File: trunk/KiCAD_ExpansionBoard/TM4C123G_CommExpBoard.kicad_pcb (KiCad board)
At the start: 2 copper layers, 50.8 x 58.4 mm, 58 parts, among them J1 TI_BOOSTER_40_J1, J2 TI_BOOSTER_40_J2, J3 TI_BOOSTER_40_J3, J4 TI_BOOSTER_40_J4, P1 ANT_GND, P10 GPIO0, P5 ANT_C, P6 CAN, P7 UART1, P8 RS485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

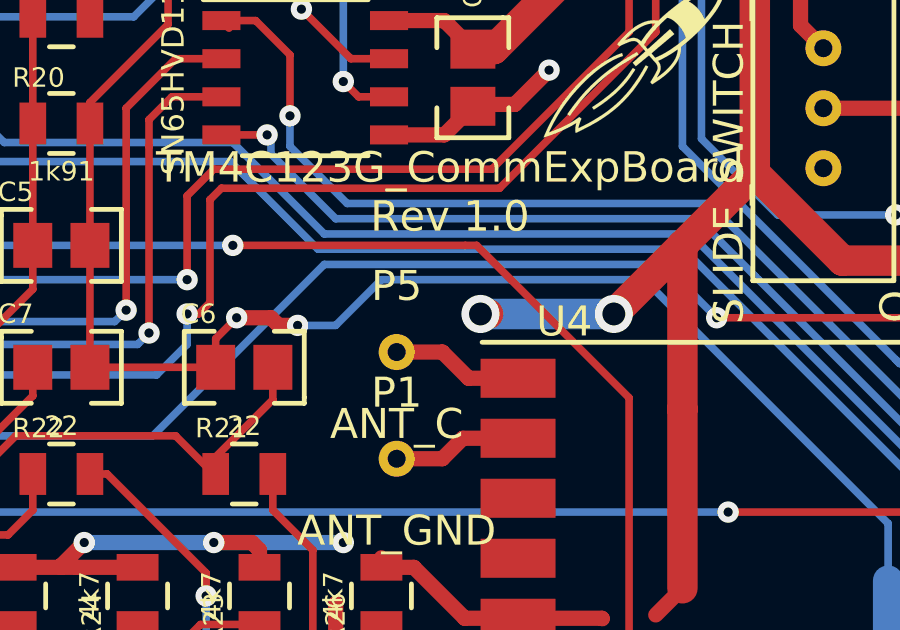
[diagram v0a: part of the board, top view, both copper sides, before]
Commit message: moved P1 and P5 silkscreens near relative pads.
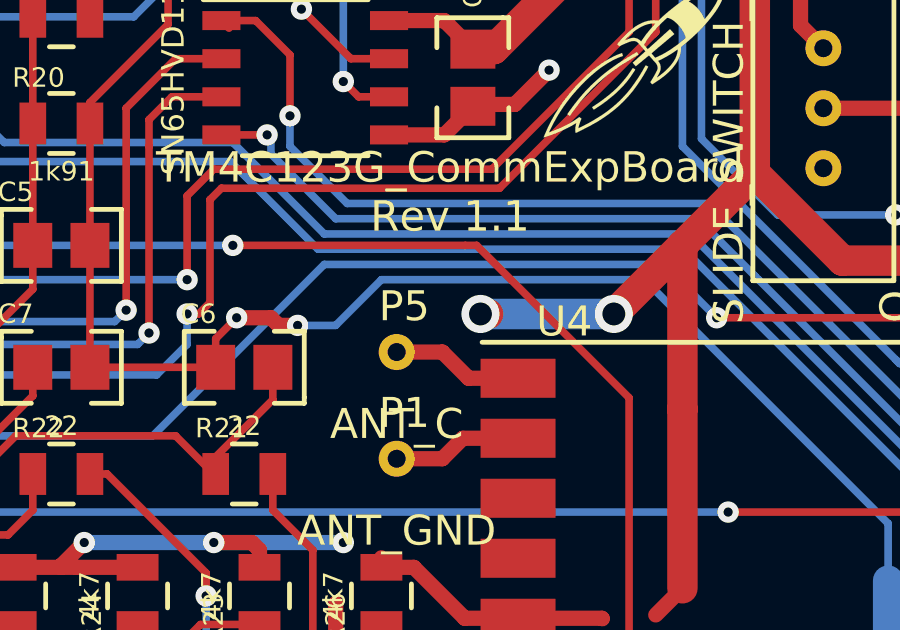
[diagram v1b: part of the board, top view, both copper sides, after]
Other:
- board text added: "TM4C123G_CommExpBoard Rev 1.1"
- board text removed: "TM4C123G_CommExpBoard Rev 1.0"
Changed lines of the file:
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@@
     (links 139)
     (no_connects 0)
-    (area 125.649999 57.069999 176.610001 115.650001)
+    (area 108.280288 51.989999 181.690001 123.604001)
     (thickness 1.6)
     (drawings 57)
@@
   (title_block
     (title "TM4C123G Communication Expansion Board")
-    (rev 1.0)
+    (rev 1.1)
     (company "Luca Buccolini, Student @ Università Politecnica delle Marche")
     (comment 1 "Expansion Board for the Texas Instruments TM4C123G Launchpad ")
@@
   (module ANT_PAD_MD (layer F.Cu)
     (at 147.066 102.362)
-    (fp_text reference P1 (at 0 -2.2) (layer F.SilkS)
+    (fp_text reference P1 (at 0.254 -1.524) (layer F.SilkS)
       (effects (font (size 1 1) (thickness 0.15)))
     )
@@
   (module ANT_PAD_MD (layer F.Cu)
     (at 147.066 98.806)
-    (fp_text reference P5 (at 0 -2.2) (layer F.SilkS)
+    (fp_text reference P5 (at 0.254 -1.524) (layer F.SilkS)
       (effects (font (size 1 1) (thickness 0.15)))
     )
@@
     (effects (font (size 0.762 0.762) (thickness 0.15875)))
   )
-  (gr_text "TM4C123G_CommExpBoard \nRev 1.0" (at 148.844 93.472) (layer F.SilkS)
+  (gr_text "TM4C123G_CommExpBoard \nRev 1.1" (at 148.844 93.472) (layer F.SilkS)
     (effects (font (size 1.016 1.016) (thickness 0.15875)))
   )

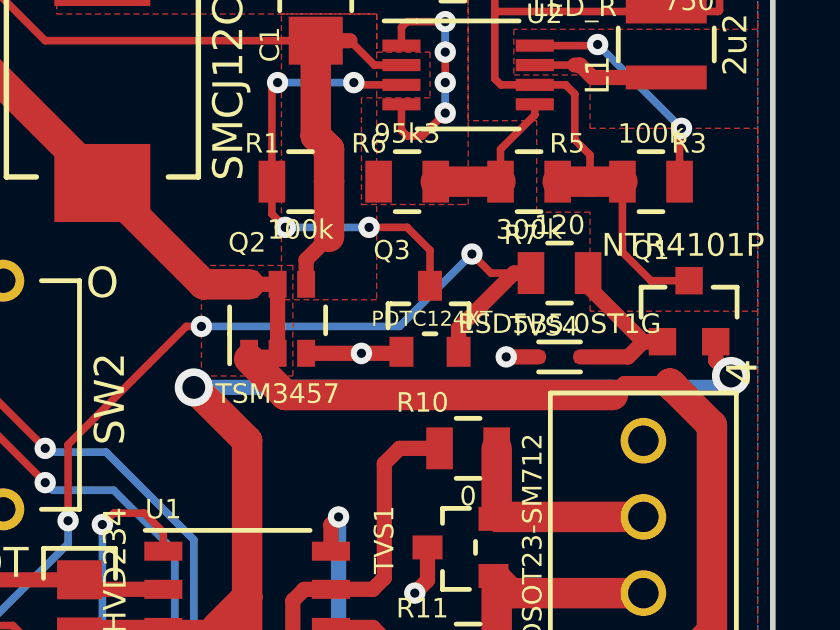
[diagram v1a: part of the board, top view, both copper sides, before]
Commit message: Update of PCB and schematic to rev 1.1 (fixed old Q3 footprint in which pins 1 and 2 were flipped and relative nets). Build new v1.1 fabrication files.
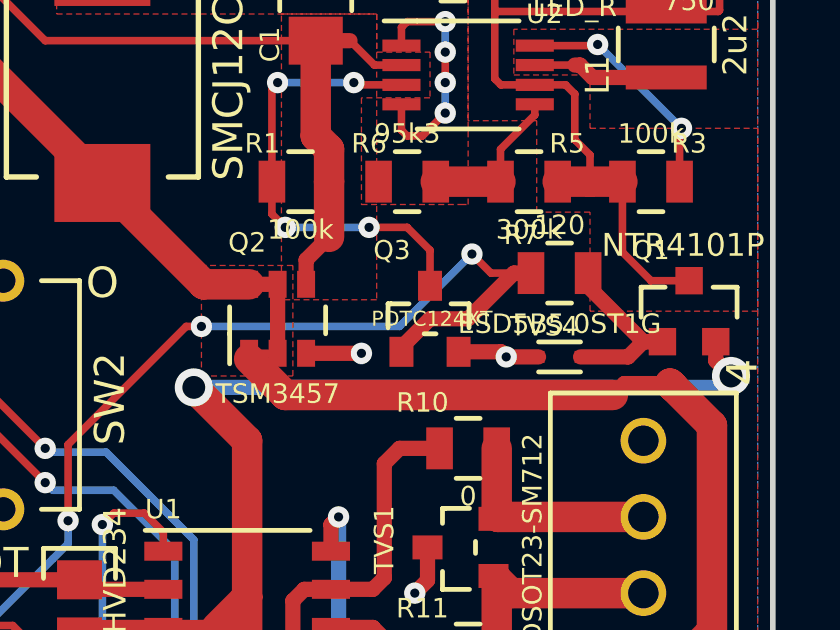
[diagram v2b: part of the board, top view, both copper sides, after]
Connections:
- Q3 pad 1: GND -> +5V_TLP
- Q3 pad 2: +5V_TLP -> GND
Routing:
- net +5V_TLP: track 52.8 -> 54.3 mm
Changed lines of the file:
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@@
     (thickness 1.6)
     (drawings 57)
-    (tracks 732)
+    (tracks 734)
     (zones 0)
     (modules 58)
@@
   (layers
     (15 F.Cu signal)
-    (0 B.Cu signal)
+    (0 B.Cu signal hide)
     (16 B.Adhes user)
     (17 F.Adhes user)
@@
       (drillshape 0)
       (scaleselection 1)
-      (outputdirectory PCB_fabrication/Drill/))
+      (outputdirectory PCB_fabrication/Gerber/))
   )
   (net 0 "")
@@
     (pad 2 smd rect (at 0.9525 1.09982) (size 0.8001 1.00076)
       (layers F.Cu F.Paste F.Mask)
-      (net 3 +5V_TLP)
+      (net 43 GND)
     )
     (pad 1 smd rect (at -0.9525 1.09982) (size 0.8001 1.00076)
       (layers F.Cu F.Paste F.Mask)
-      (net 43 GND)
+      (net 3 +5V_TLP)
     )
     (model smd\SOT23_3.wrl
@@
   (segment (start 156.21 81.661) (end 153.7335 81.661) (width 0.508) (layer F.Cu) (net 2))
   (segment (start 153.7335 81.661) (end 153.416 81.9785) (width 0.508) (layer F.Cu) (net 2))
-  (segment (start 148.59 84.582) (end 149.352 84.582) (width 0.254) (layer F.Cu) (net 3))
   (segment (start 152.527 79.375) (end 153.035 78.867) (width 0.254) (layer B.Cu) (net 3))
   (segment (start 153.035 78.867) (end 153.035 78.105) (width 0.254) (layer B.Cu) (net 3))
@@
   (segment (start 150.368 81.534) (end 152.527 79.375) (width 0.254) (layer B.Cu) (net 3))
   (segment (start 150.368 82.55) (end 150.368 81.534) (width 0.254) (layer B.Cu) (net 3))
+  (segment (start 164.1475 72.47382) (end 164.1475 72.3265) (width 0.508) (layer F.Cu) (net 3))
+  (segment (start 167.894 69.85) (end 168.4655 69.85) (width 0.508) (layer F.Cu) (net 3))
+  (segment (start 166.37 71.374) (end 167.894 69.85) (width 0.508) (layer F.Cu) (net 3))
+  (segment (start 165.1 71.374) (end 166.37 71.374) (width 0.508) (layer F.Cu) (net 3))
+  (segment (start 164.1475 72.3265) (end 165.1 71.374) (width 0.508) (layer F.Cu) (net 3))
+  (segment (start 148.59 84.582) (end 149.352 84.582) (width 0.254) (layer F.Cu) (net 3))
   (segment (start 150.368 82.55) (end 150.368 82.55) (width 0.254) (layer B.Cu) (net 3))
   (via (at 150.368 82.55) (size 0.7112) (layers F.Cu B.Cu) (net 3))
@@
   (segment (start 141.351 84.582) (end 138.303 87.63) (width 0.254) (layer B.Cu) (net 3))
   (segment (start 130.81 87.63) (end 138.303 87.63) (width 0.254) (layer B.Cu) (net 3))
-  (segment (start 166.0525 72.47382) (end 166.0525 71.6915) (width 0.508) (layer F.Cu) (net 3))
-  (segment (start 166.0525 71.6915) (end 167.894 69.85) (width 0.508) (layer F.Cu) (net 3))
-  (segment (start 167.894 69.85) (end 168.4655 69.85) (width 0.508) (layer F.Cu) (net 3))
   (segment (start 161.798 82.931) (end 163.195 82.931) (width 0.254) (layer F.Cu) (net 4))
   (segment (start 172.72 99.06) (end 173.99 100.33) (width 0.254) (layer F.Cu) (net 4))
@@
   (segment (start 131.318 102.87) (end 133.604 100.584) (width 0.254) (layer F.Cu) (net 42))
   (segment (start 130.81 102.87) (end 130.81 102.87) (width 0.254) (layer F.Cu) (net 42))
+  (segment (start 166.0525 72.47382) (end 167.46982 72.47382) (width 0.508) (layer F.Cu) (net 43))
+  (via (at 167.64 72.644) (size 0.7112) (layers F.Cu B.Cu) (net 43))
+  (segment (start 167.64 72.644) (end 168.718 72.644) (width 0.508) (layer F.Cu) (net 43))
+  (segment (start 167.46982 72.47382) (end 167.64 72.644) (width 0.508) (layer F.Cu) (net 43))
+  (via (at 162.814 72.524) (size 0.7112) (layers F.Cu B.Cu) (net 43))
+  (segment (start 162.814 72.524) (end 162.814 72.644) (width 0.508) (layer B.Cu) (net 43))
   (segment (start 163.449 106.426) (end 163.449 104.521) (width 0.254) (layer B.Cu) (net 43))
   (segment (start 142.875 97.663) (end 143.129 97.917) (width 0.508) (layer F.Cu) (net 43))
@@
   (segment (start 156.21 80.391) (end 153.7335 80.391) (width 0.508) (layer F.Cu) (net 43))
   (segment (start 153.7335 80.391) (end 153.416 80.0735) (width 0.508) (layer F.Cu) (net 43))
-  (segment (start 168.718 72.644) (end 167.64 72.644) (width 0.508) (layer F.Cu) (net 43))
-  (via (at 167.64 72.644) (size 0.7112) (layers F.Cu B.Cu) (net 43))
-  (via (at 162.814 72.524) (size 0.7112) (layers F.Cu B.Cu) (net 43))
-  (segment (start 162.814 72.524) (end 162.814 72.644) (width 0.508) (layer B.Cu) (net 43))
   (segment (start 165.01618 78.994) (end 165.01618 80.09382) (width 0.508) (layer F.Cu) (net 43))
   (via (at 164.592 80.518) (size 0.7112) (layers F.Cu B.Cu) (net 43))
   (segment (start 165.01618 80.09382) (end 164.592 80.518) (width 0.508) (layer F.Cu) (net 43))
   (segment (start 160.97 72.524) (end 162.814 72.524) (width 0.508) (layer F.Cu) (net 43))
-  (segment (start 162.814 72.524) (end 164.09732 72.524) (width 0.508) (layer F.Cu) (net 43))
-  (segment (start 164.09732 72.524) (end 164.1475 72.47382) (width 0.508) (layer F.Cu) (net 43))
   (segment (start 164.1475 62.2681) (end 164.1475 61.6585) (width 0.254) (layer F.Cu) (net 43))
   (segment (start 164.1475 65.0875) (end 164.1475 64.2239) (width 0.254) (layer F.Cu) (net 43))
